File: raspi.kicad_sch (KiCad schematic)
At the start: 59 parts, among them J8 Conn_01x03, J9 debug_probe, SW1 SW_Omron_B3FS, U6 RP2350B-QFN80, U8 16Mbit PSRAM, X1 ASE-12.000MHZ-L-C-T

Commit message: footprint cleanup
switched to 0402 resistors, updated connectors, etc...
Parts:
- J8: footprint Connector_PinHeader_2.54mm:PinHeader_1x03_P2.54mm_Vertical_SMD_Pin1Left -> Connector_PinHeader_2.54mm:PinHeader_1x03_P2.54mm_Vertical
- R24, R25, R26, R27, R32, R33, R34, R35, R36, R41, R43, R44, R45, R46, R47, R48, R49: footprint Resistor_SMD:R_0603_1608Metric -> Resistor_SMD:R_0402_1005Metric
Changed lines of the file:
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@@
 			)
 		)
-		(property "Footprint" "Resistor_SMD:R_0603_1608Metric"
+		(property "Footprint" "Resistor_SMD:R_0402_1005Metric"
 			(at 60.96 36.83 0)
 			(effects
@@
 			)
 		)
-		(property "Footprint" "Resistor_SMD:R_0603_1608Metric"
+		(property "Footprint" "Resistor_SMD:R_0402_1005Metric"
 			(at 157.48 44.45 0)
 			(effects
@@
 			)
 		)
-		(property "Footprint" "Resistor_SMD:R_0603_1608Metric"
+		(property "Footprint" "Resistor_SMD:R_0402_1005Metric"
 			(at 30.48 148.59 0)
 			(effects
@@
 			)
 		)
-		(property "Footprint" "Connector_PinHeader_2.54mm:PinHeader_1x03_P2.54mm_Vertical_SMD_Pin1Left"
+		(property "Footprint" "Connector_PinHeader_2.54mm:PinHeader_1x03_P2.54mm_Vertical"
 			(at 267.97 21.59 0)
 			(effects
@@
 			)
 		)
-		(property "Footprint" "Resistor_SMD:R_0603_1608Metric"
+		(property "Footprint" "Resistor_SMD:R_0402_1005Metric"
 			(at 30.48 143.51 0)
 			(effects
@@
 			)
 		)
-		(property "Footprint" "Resistor_SMD:R_0603_1608Metric"
+		(property "Footprint" "Resistor_SMD:R_0402_1005Metric"
 			(at 162.56 163.83 0)
 			(effects
@@
 			)
 		)
-		(property "Footprint" "Resistor_SMD:R_0603_1608Metric"
+		(property "Footprint" "Resistor_SMD:R_0402_1005Metric"
 			(at 21.59 101.6 0)
 			(effects
@@
 			)
 		)
-		(property "Footprint" "Resistor_SMD:R_0603_1608Metric"
+		(property "Footprint" "Resistor_SMD:R_0402_1005Metric"
 			(at 243.84 19.05 0)
 			(effects
@@
 			)
 		)
-		(property "Footprint" "Resistor_SMD:R_0603_1608Metric"
+		(property "Footprint" "Resistor_SMD:R_0402_1005Metric"
 			(at 162.56 161.29 0)
 			(effects
@@
 			)
 		)
-		(property "Footprint" "Resistor_SMD:R_0603_1608Metric"
+		(property "Footprint" "Resistor_SMD:R_0402_1005Metric"
 			(at 139.7 21.59 0)
 			(effects
@@
 			)
 		)
-		(property "Footprint" "Resistor_SMD:R_0603_1608Metric"
+		(property "Footprint" "Resistor_SMD:R_0402_1005Metric"
 			(at 162.56 166.37 0)
 			(effects
@@
 			)
 		)
-		(property "Footprint" "Resistor_SMD:R_0603_1608Metric"
+		(property "Footprint" "Resistor_SMD:R_0402_1005Metric"
 			(at 243.84 21.59 0)
 			(effects
@@
 			)
 		)
-		(property "Footprint" "Resistor_SMD:R_0603_1608Metric"
+		(property "Footprint" "Resistor_SMD:R_0402_1005Metric"
 			(at 157.48 46.99 0)
 			(effects
@@
 			)
 		)
-		(property "Footprint" "Resistor_SMD:R_0603_1608Metric"
+		(property "Footprint" "Resistor_SMD:R_0402_1005Metric"
 			(at 250.19 143.51 0)
 			(effects
@@
 			)
 		)
-		(property "Footprint" "Resistor_SMD:R_0603_1608Metric"
+		(property "Footprint" "Resistor_SMD:R_0402_1005Metric"
 			(at 243.84 35.56 0)
 			(effects
@@
 			)
 		)
-		(property "Footprint" "Resistor_SMD:R_0603_1608Metric"
+		(property "Footprint" "Resistor_SMD:R_0402_1005Metric"
 			(at 54.61 62.23 0)
 			(effects
@@
 			)
 		)
-		(property "Footprint" "Resistor_SMD:R_0603_1608Metric"
+		(property "Footprint" "Resistor_SMD:R_0402_1005Metric"
 			(at 243.84 33.02 0)
 			(effects
@@
 			)
 		)
-		(property "Footprint" "Resistor_SMD:R_0603_1608Metric"
+		(property "Footprint" "Resistor_SMD:R_0402_1005Metric"
 			(at 162.56 158.75 0)
 			(effects

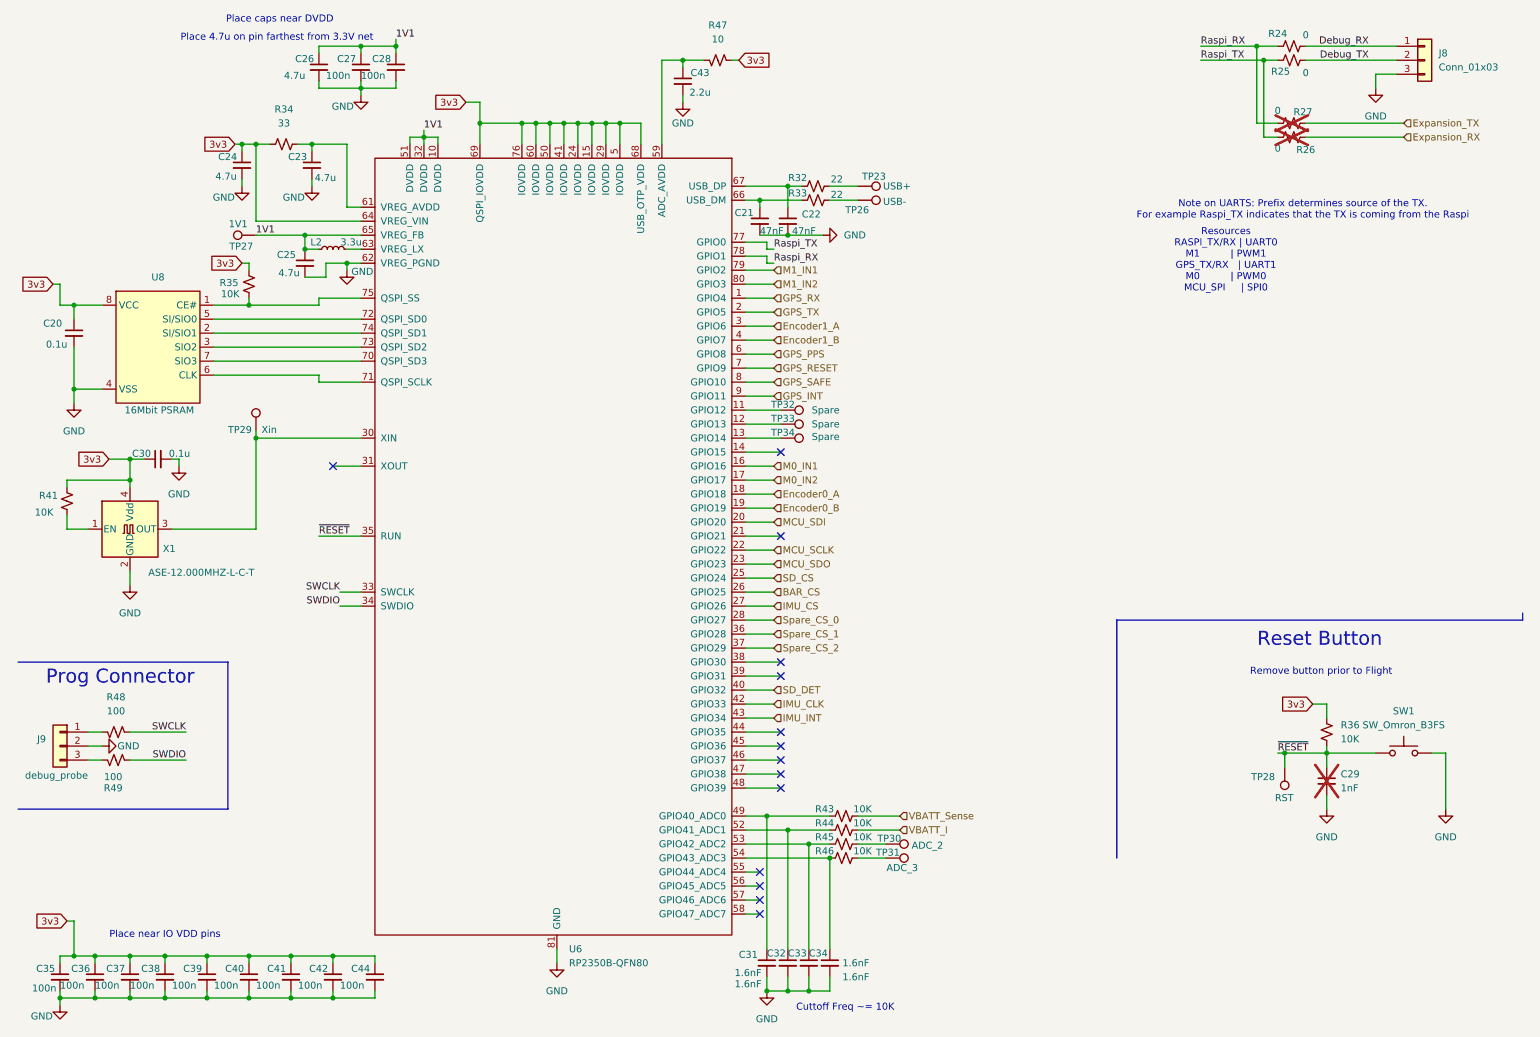
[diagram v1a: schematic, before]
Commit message: Added USB C Connector
Added usb C connector, consolidated ESD parts, cleaned up footprint selection.
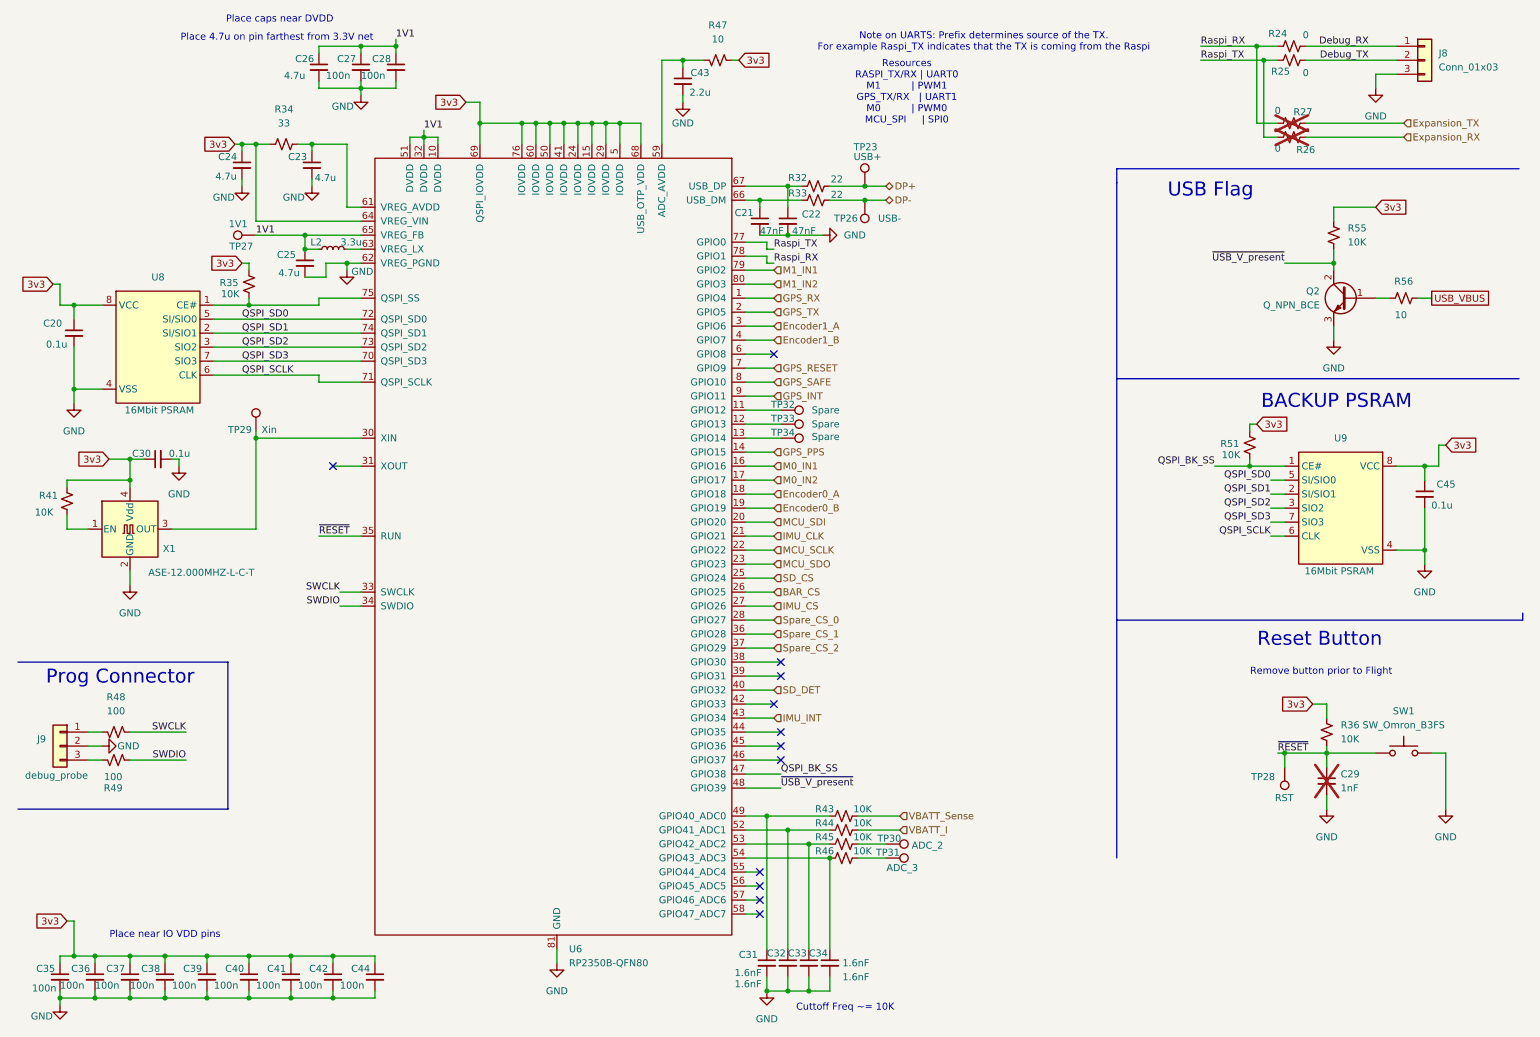
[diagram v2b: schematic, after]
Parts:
- added C45: 0.1u, Capacitor_SMD:C_0603_1608Metric_Pad1.08x0.95mm_HandSolder, symbol Device:C_Small
- added Q2: Q_NPN_BCE, Package_TO_SOT_SMD:SOT-23-3, symbol Device:Q_NPN_BCE
- added R51, R55: 10K, Resistor_SMD:R_0402_1005Metric, symbol Device:R_Small_US
- added R56: 10, Resistor_SMD:R_0402_1005Metric, symbol Device:R_Small_US
- added U9: 16Mbit PSRAM, Package_SO:SOIC-8_3.9x4.9mm_P1.27mm, symbol IS6xWVS2M8xLL:IS6xWVS2M8xLL
- J9: footprint Connector_JST:JST_SH_SM03B-SRSS-TB_1x03-1MP_P1.00mm_Horizontal -> Connector_JST:JST_SH_BM03B-SRSS-TB_1x03-1MP_P1.00mm_Vertical
- U8: footprint Package_SO:SOIC-8-1EP_3.9x4.9mm_P1.27mm_EP2.29x3mm -> Package_SO:SOIC-8_3.9x4.9mm_P1.27mm
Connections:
- net 3v3: now also C45.1, R51.1, R55.1, U9.8 (VCC)
- net GND: now also C45.2, Q2.3 (E), U9.4 (VSS)
- net GPS_PPS: now also U6.14 (GPIO15); no longer U6.6 (GPIO8)
- net IMU_CLK: now also U6.21 (GPIO21); no longer U6.42 (GPIO33)
- net DP+: now reaches R32.2, TP23.1
- net DP-: now reaches R33.2, TP26.1
- net QSPI_BK_SS: now reaches U6.47 (GPIO38)
- net QSPI_BK_SS: now also R51.2, U9.1 (CE#)
- net ~{USB_V_present}: now reaches U6.48 (GPIO39)
- net ~{USB_V_present}: now also Q2.2 (C), R55.2
- net QSPI_SD3: now reaches U6.70 (QSPI_SD3), U8.7 (SIO3)
- net QSPI_SD3: now also U9.7 (SIO3)
- net QSPI_SCLK: now reaches U6.71 (QSPI_SCLK), U8.6 (CLK)
- net QSPI_SCLK: now also U9.6 (CLK)
- net QSPI_SD0: now reaches U6.72 (QSPI_SD0), U8.5 (SI/SIO0)
- net QSPI_SD0: now also U9.5 (SI/SIO0)
- net QSPI_SD2: now reaches U6.73 (QSPI_SD2), U8.3 (SIO2)
- net QSPI_SD2: now also U9.3 (SIO2)
- net QSPI_SD1: now reaches U6.74 (QSPI_SD1), U8.2 (SI/SIO1)
- net QSPI_SD1: now also U9.2 (SI/SIO1)
- new net: Q2.1 (B), R56.1
- new net USB_VBUS: R56.2
- no-connect marks 14 -> 12
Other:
- note added: "BACKUP PSRAM"
- note added: "USB Flag"
- moved on the sheet: TP23, TP26

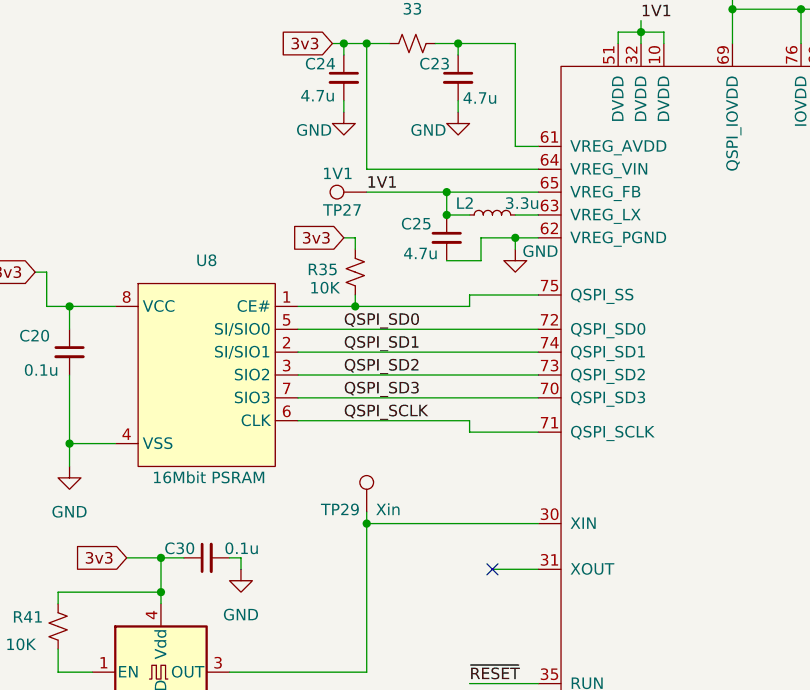
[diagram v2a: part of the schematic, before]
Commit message: Layout updates
testpoints, usb power, etc.
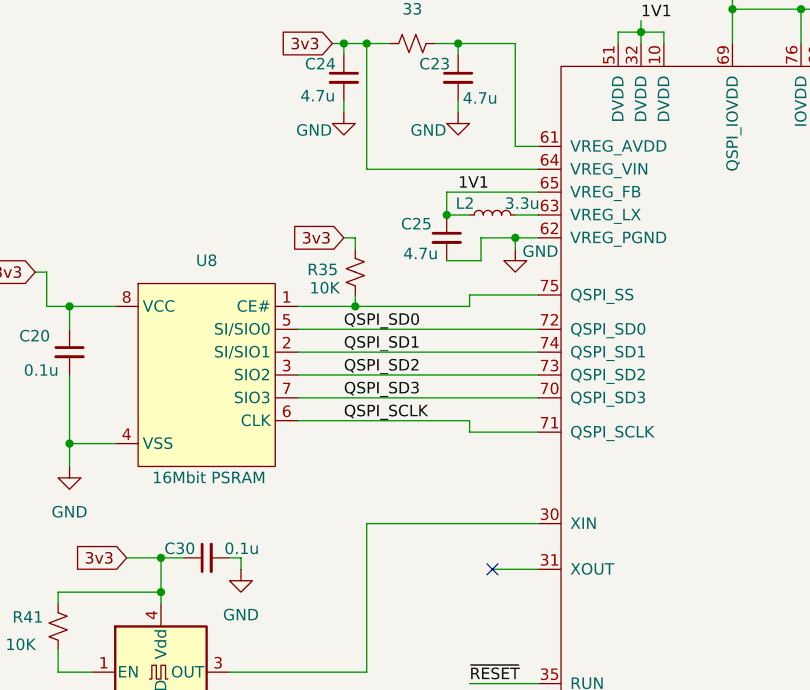
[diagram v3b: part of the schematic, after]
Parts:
- removed TP27: 1V1, TestPoint:TestPoint_Pad_1.0x1.0mm, symbol Connector:TestPoint
- removed TP29: Xin, TestPoint:TestPoint_Pad_1.0x1.0mm, symbol Connector:TestPoint
- TP23, TP26, TP28, TP30, TP31, TP32, TP33, TP34: footprint TestPoint:TestPoint_Pad_1.0x1.0mm -> TestPoint:TestPoint_Pad_D1.0mm
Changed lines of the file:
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@@
 	)
 	(junction
-		(at 64.77 53.34)
-		(diameter 0)
-		(color 0 0 0 0)
-	)
-	(junction
 		(at 251.46 58.42)
 		(diameter 0)
@@
 	)
 	(junction
-		(at 55.88 90.17)
-		(diameter 0)
-		(color 0 0 0 0)
-	)
-	(junction
 		(at 111.76 33.02)
 		(diameter 0)
@@
 	(wire
 		(pts
-			(xy 55.88 88.9) (xy 55.88 90.17)
-		)
-		(stroke
-			(width 0)
-			(type default)
-		)
-	)
-	(wire
-		(pts
 			(xy 53.34 43.18) (xy 53.34 44.45)
 		)
@@
 	(wire
 		(pts
-			(xy 55.88 53.34) (xy 64.77 53.34)
-		)
-		(stroke
-			(width 0)
-			(type default)
-		)
-	)
-	(wire
-		(pts
 			(xy 144.78 82.55) (xy 149.86 82.55)
 		)
@@
 	)
 	(label "1V1"
-		(at 55.88 53.34 0)
+		(at 66.04 53.34 0)
 		(fields_autoplaced yes)
 		(effects
@@
 			)
 		)
-		(property "Footprint" "TestPoint:TestPoint_Pad_1.0x1.0mm"
+		(property "Footprint" "TestPoint:TestPoint_Pad_D1.0mm"
 			(at 170.18 168.91 0)
 			(effects
@@
 			)
 		)
-		(property "Footprint" "TestPoint:TestPoint_Pad_1.0x1.0mm"
+		(property "Footprint" "TestPoint:TestPoint_Pad_D1.0mm"
 			(at 151.13 95.25 0)
 			(effects
@@
 			)
 		)
-		(property "Footprint" "TestPoint:TestPoint_Pad_1.0x1.0mm"
+		(property "Footprint" "TestPoint:TestPoint_Pad_D1.0mm"
 			(at 170.18 171.45 0)
 			(effects
@@
 	)
 	(symbol
-		(lib_id "Connector:TestPoint")
-		(at 55.88 53.34 90)
-		(unit 1)
-		(exclude_from_sim no)
-		(in_bom yes)
-		(on_board yes)
-		(dnp no)
-		(property "Reference" "TP27"
-			(at 55.372 55.372 90)
-			(effects
-				(font
-					(size 1.27 1.27)
-				)
-				(justify left)
-			)
-		)
-		(property "Value" "1V1"
-			(at 54.356 51.308 90)
-			(effects
-				(font
-					(size 1.27 1.27)
-				)
-				(justify left)
-			)
-		)
-		(property "Footprint" "TestPoint:TestPoint_Pad_1.0x1.0mm"
-			(at 55.88 48.26 0)
-			(effects
-				(font
-					(size 1.27 1.27)
-				)
-				(hide yes)
-			)
-		)
-		(property "Datasheet" "~"
-			(at 55.88 48.26 0)
-			(effects
-				(font
-					(size 1.27 1.27)
-				)
-				(hide yes)
-			)
-		)
-		(property "Description" "test point"
-			(at 55.88 53.34 0)
-			(effects
-				(font
-					(size 1.27 1.27)
-				)
-				(hide yes)
-			)
-		)
-		(pin "1"
-		)
-		(instances
-			(project "moon_child"
-				(path "/9fe08eae-9310-46cf-b272-eac4209a7b3e/95a2c5f2-1168-40e1-9976-12a9d3efcb94"
-					(reference "TP27")
-					(unit 1)
-				)
-			)
-		)
-	)
-	(symbol
 		(lib_id "Switch:SW_Omron_B3FS")
 		(at 264.16 147.32 0)
@@
 			)
 		)
-		(property "Footprint" "TestPoint:TestPoint_Pad_1.0x1.0mm"
+		(property "Footprint" "TestPoint:TestPoint_Pad_D1.0mm"
 			(at 151.13 90.17 0)
 			(effects
@@
 			)
 		)
-		(property "Footprint" "TestPoint:TestPoint_Pad_1.0x1.0mm"
+		(property "Footprint" "TestPoint:TestPoint_Pad_D1.0mm"
 			(at 171.45 44.45 0)
 			(effects
@@
 			)
 		)
-		(property "Footprint" "TestPoint:TestPoint_Pad_1.0x1.0mm"
+		(property "Footprint" "TestPoint:TestPoint_Pad_D1.0mm"
 			(at 161.29 46.99 0)
 			(effects
@@
 	)
 	(symbol
-		(lib_id "Connector:TestPoint")
-		(at 55.88 88.9 0)
-		(unit 1)
-		(exclude_from_sim no)
-		(in_bom yes)
-		(on_board yes)
-		(dnp no)
-		(property "Reference" "TP29"
-			(at 50.8 88.646 0)
-			(effects
-				(font
-					(size 1.27 1.27)
-				)
-				(justify left)
-			)
-		)
-		(property "Value" "Xin"
-			(at 56.896 88.646 0)
-			(effects
-				(font
-					(size 1.27 1.27)
-				)
-				(justify left)
-			)
-		)
-		(property "Footprint" "TestPoint:TestPoint_Pad_1.0x1.0mm"
-			(at 60.96 88.9 0)
-			(effects
-				(font
-					(size 1.27 1.27)
-				)
-				(hide yes)
-			)
-		)
-		(property "Datasheet" "~"
-			(at 60.96 88.9 0)
-			(effects
-				(font
-					(size 1.27 1.27)
-				)
-				(hide yes)
-			)
-		)
-		(property "Description" "test point"
-			(at 55.88 88.9 0)
-			(effects
-				(font
-					(size 1.27 1.27)
-				)
-				(hide yes)
-			)
-		)
-		(pin "1"
-		)
-		(instances
-			(project ""
-				(path "/9fe08eae-9310-46cf-b272-eac4209a7b3e/95a2c5f2-1168-40e1-9976-12a9d3efcb94"
-					(reference "TP29")
-					(unit 1)
-				)
-			)
-		)
-	)
-	(symbol
 		(lib_id "power:GND")
 		(at 271.78 157.48 0)
@@
 			)
 		)
-		(property "Footprint" "TestPoint:TestPoint_Pad_1.0x1.0mm"
+		(property "Footprint" "TestPoint:TestPoint_Pad_D1.0mm"
 			(at 151.13 92.71 0)
 			(effects
@@
 			)
 		)
-		(property "Footprint" "TestPoint:TestPoint_Pad_1.0x1.0mm"
+		(property "Footprint" "TestPoint:TestPoint_Pad_D1.0mm"
 			(at 237.49 149.86 0)
 			(effects

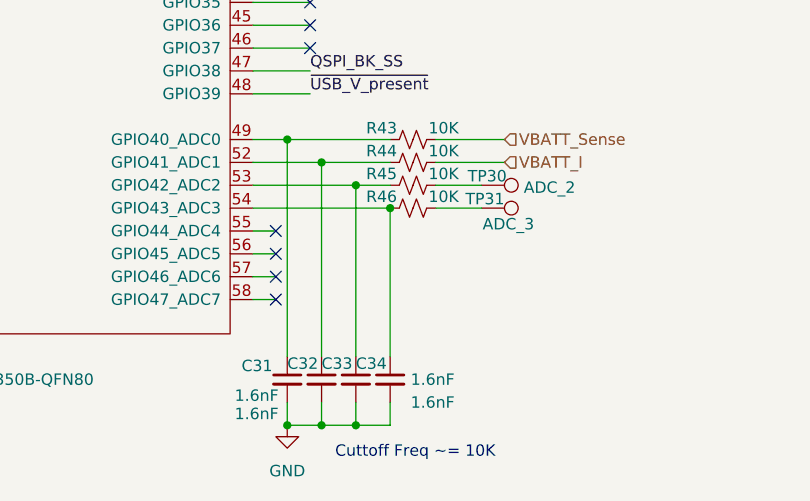
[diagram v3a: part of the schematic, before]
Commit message: layout updates
removes ADC 2 and ADC 3 connections for space reasons
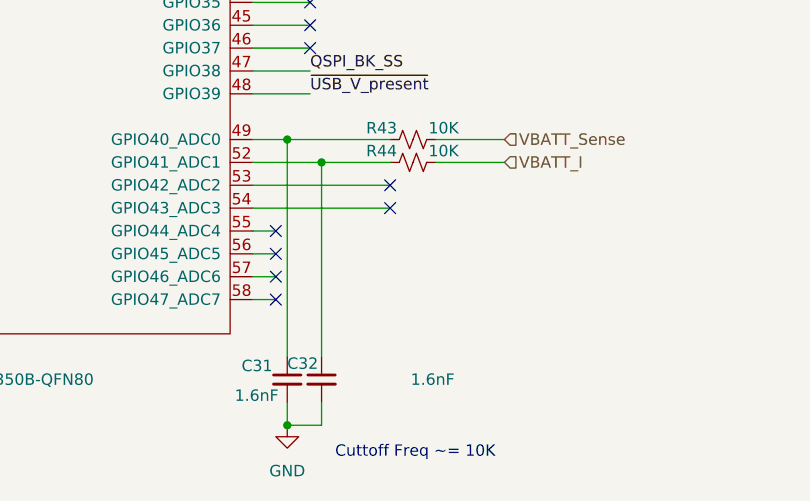
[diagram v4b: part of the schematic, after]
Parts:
- removed C33, C34: 1.6nF, Capacitor_SMD:C_0603_1608Metric_Pad1.08x0.95mm_HandSolder, symbol Device:C_Small
- removed R45, R46: 10K, Resistor_SMD:R_0402_1005Metric, symbol Device:R_Small_US
- removed TP30: ADC_2, TestPoint:TestPoint_Pad_D1.0mm, symbol Connector:TestPoint
- removed TP31: ADC_3, TestPoint:TestPoint_Pad_D1.0mm, symbol Connector:TestPoint
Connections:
- no-connect marks 12 -> 14
